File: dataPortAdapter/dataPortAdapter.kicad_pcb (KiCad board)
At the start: 2 copper layers, 29.5 x 24.7 mm, 6 parts, among them J1 Conn_02x05_Odd_Even, J2 Conn_02x07_Odd_Even, J3 Conn_01x07

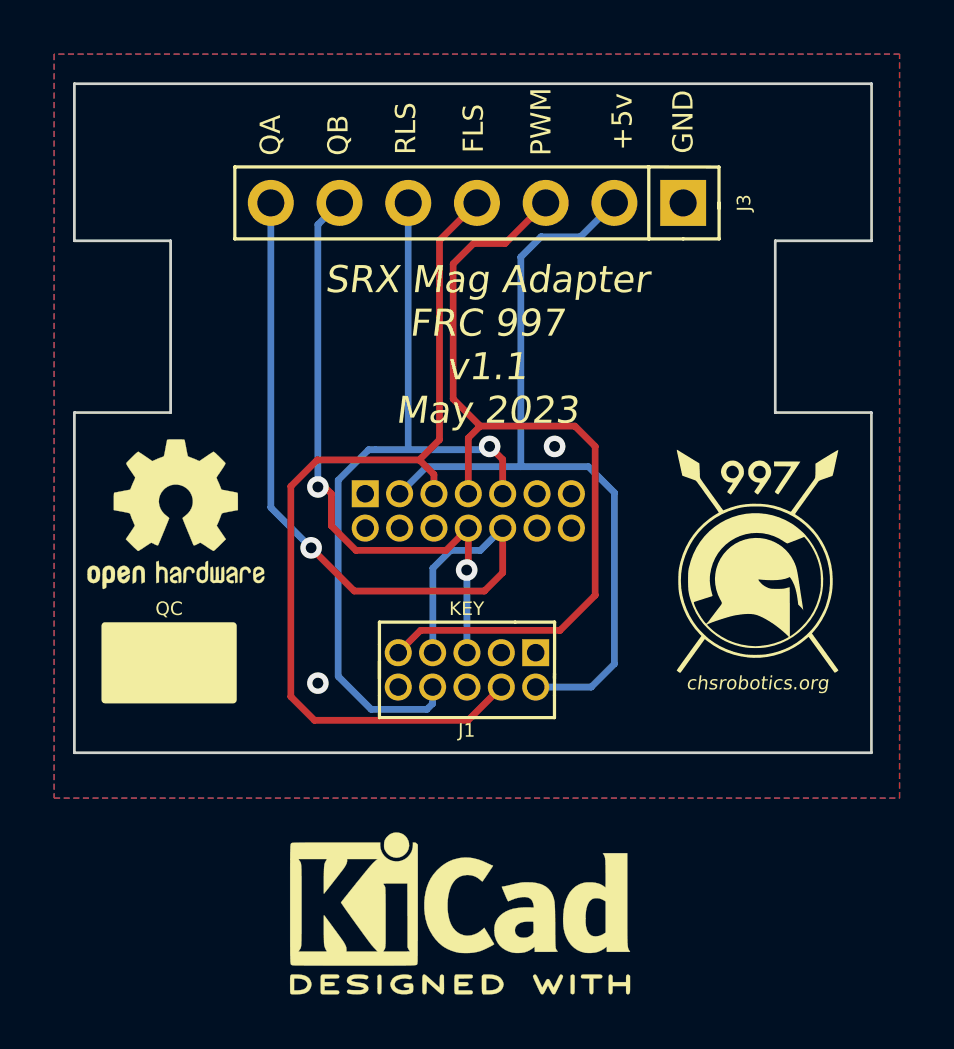
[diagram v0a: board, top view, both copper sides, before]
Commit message: Add solder jumpers to switch between modes
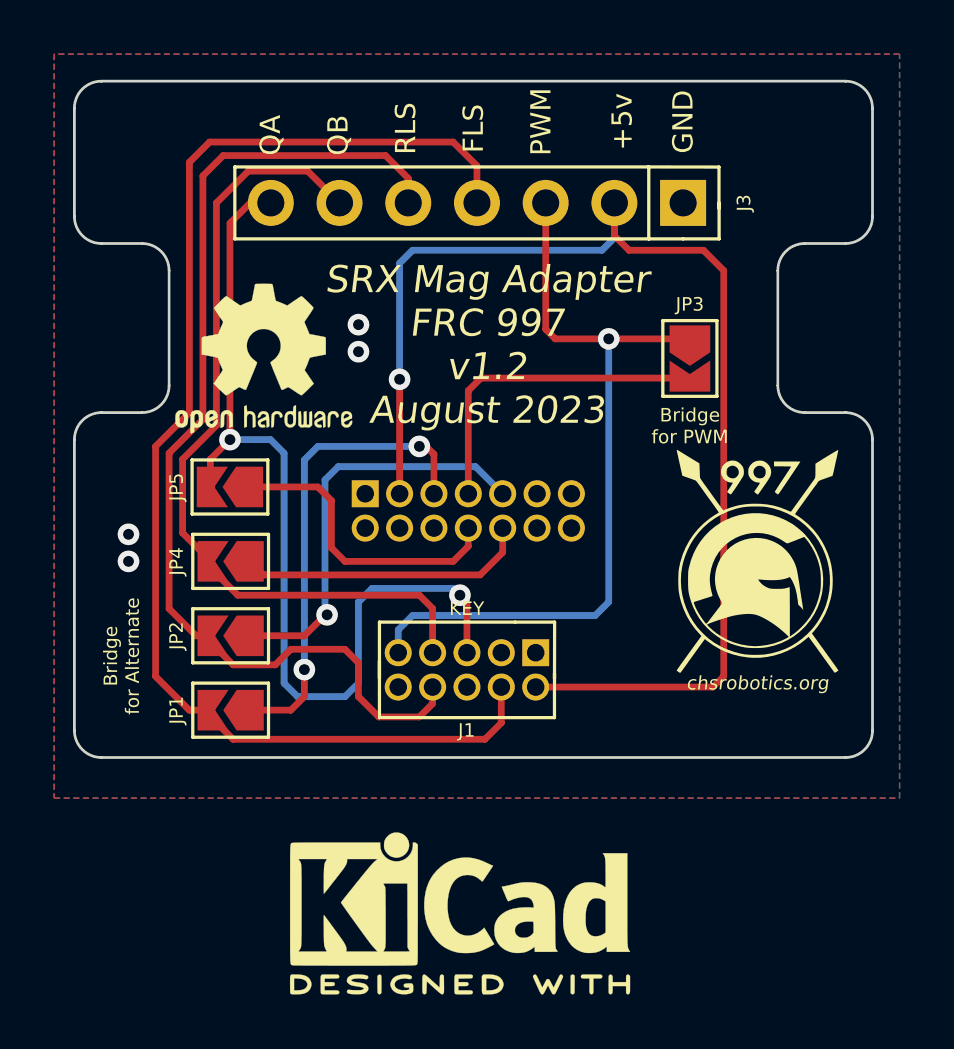
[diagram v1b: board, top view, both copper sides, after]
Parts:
- added JP1: Jumper_2_Open, Jumper:SolderJumper-2_P1.3mm_Open_TrianglePad1.0x1.5mm, F.Cu at (105.8, 111.0)
- added JP2: Jumper_2_Open, Jumper:SolderJumper-2_P1.3mm_Open_TrianglePad1.0x1.5mm, F.Cu at (105.8, 108.2)
- added JP3: Jumper_2_Bridged, Jumper:SolderJumper-2_P1.3mm_Open_TrianglePad1.0x1.5mm, F.Cu at (122.8, 98.0)
- added JP4: Jumper_2_Open, Jumper:SolderJumper-2_P1.3mm_Open_TrianglePad1.0x1.5mm, F.Cu at (105.8, 105.5)
- added JP5: Jumper_2_Open, Jumper:SolderJumper-2_P1.3mm_Open_TrianglePad1.0x1.5mm, F.Cu at (105.8, 102.8)
- moved REF** 6.60 mm to (107.0, 98.0)
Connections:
- J2 pad 10: QA -> Net-(J2-Pin_10)
- J2 pad 5: FLS -> Net-(J2-Pin_5)
- J2 pad 7: PWM -> Net-(J2-Pin_7)
- J2 pad 8: QB -> Net-(J2-Pin_8)
- J2 pad 9: RLS -> Net-(J2-Pin_9)
- J3 pad 6: QB -> QA
- J3 pad 7: QA -> QB
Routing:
- net Net-(J2-Pin_5): track 0.00 -> 17.5 mm, vias 0 -> 2
- net +5V: track 30.4 -> 46.1 mm, vias 0 -> 1
- net Net-(J2-Pin_9): track 0.00 -> 15.4 mm, vias 0 -> 1
- net FLS: track 33.4 -> 47.7 mm
- net Net-(J2-Pin_7): track 0.00 -> 12.2 mm
- net QB: track 23.0 -> 35.0 mm
- net Net-(J2-Pin_8): track 0.00 -> 11.2 mm
- net Net-(J2-Pin_10): track 0.00 -> 10.8 mm
- net RLS: track 29.1 -> 39.3 mm, vias 1 -> 0
- net PWM: track 31.7 -> 28.9 mm, vias 0 -> 1
- net QA: track 29.3 -> 30.4 mm, vias 1 -> 0
- net GND: vias 2 -> 4
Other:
- board size 29.5 x 24.7 mm -> 29.5 x 25 mm
- board text added: "Bridge for Alternate"
- board text added: "Bridge for PWM"
- board text added: "SRX Mag Adapter FRC 997 v1.2 August 2023"
- board text removed: "QC"
- board text removed: "SRX Mag Adapter FRC 997 v1.1 May 2023"
